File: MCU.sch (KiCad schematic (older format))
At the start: 32 parts, among them SW200 SW_SPDT, U200 STM32F405RGT6, U201 W25N01GVZEIG, Y200 16MHz

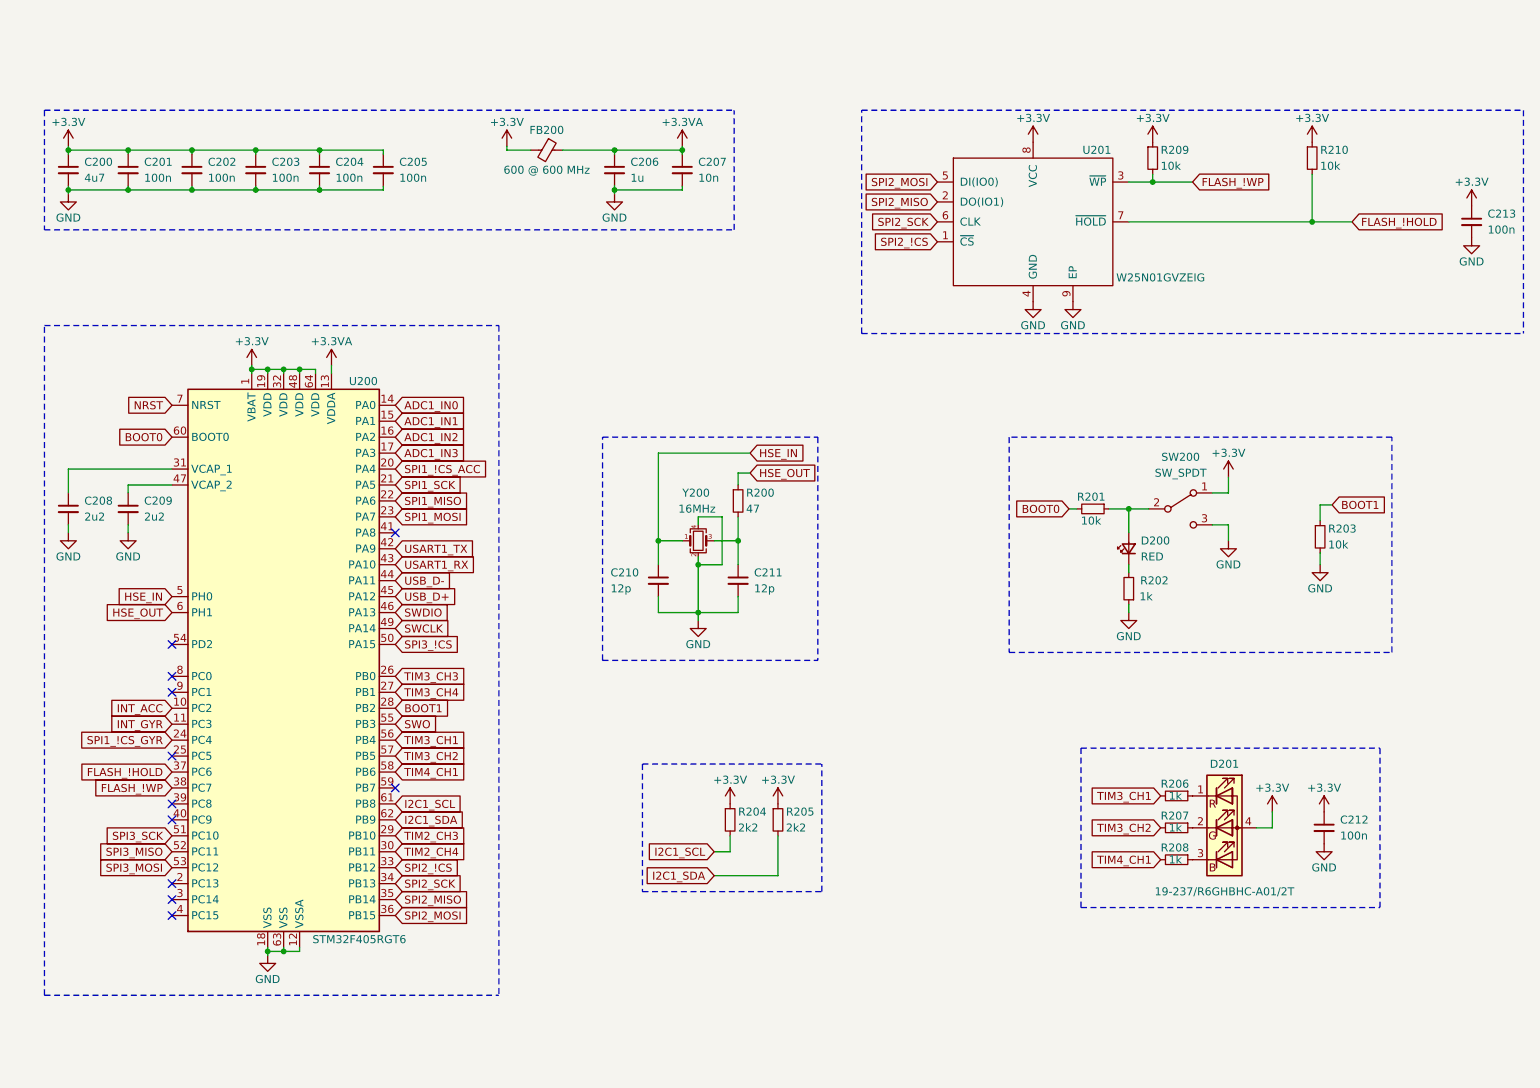
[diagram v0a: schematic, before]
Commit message: Updated firmware. Added schematic PDF.
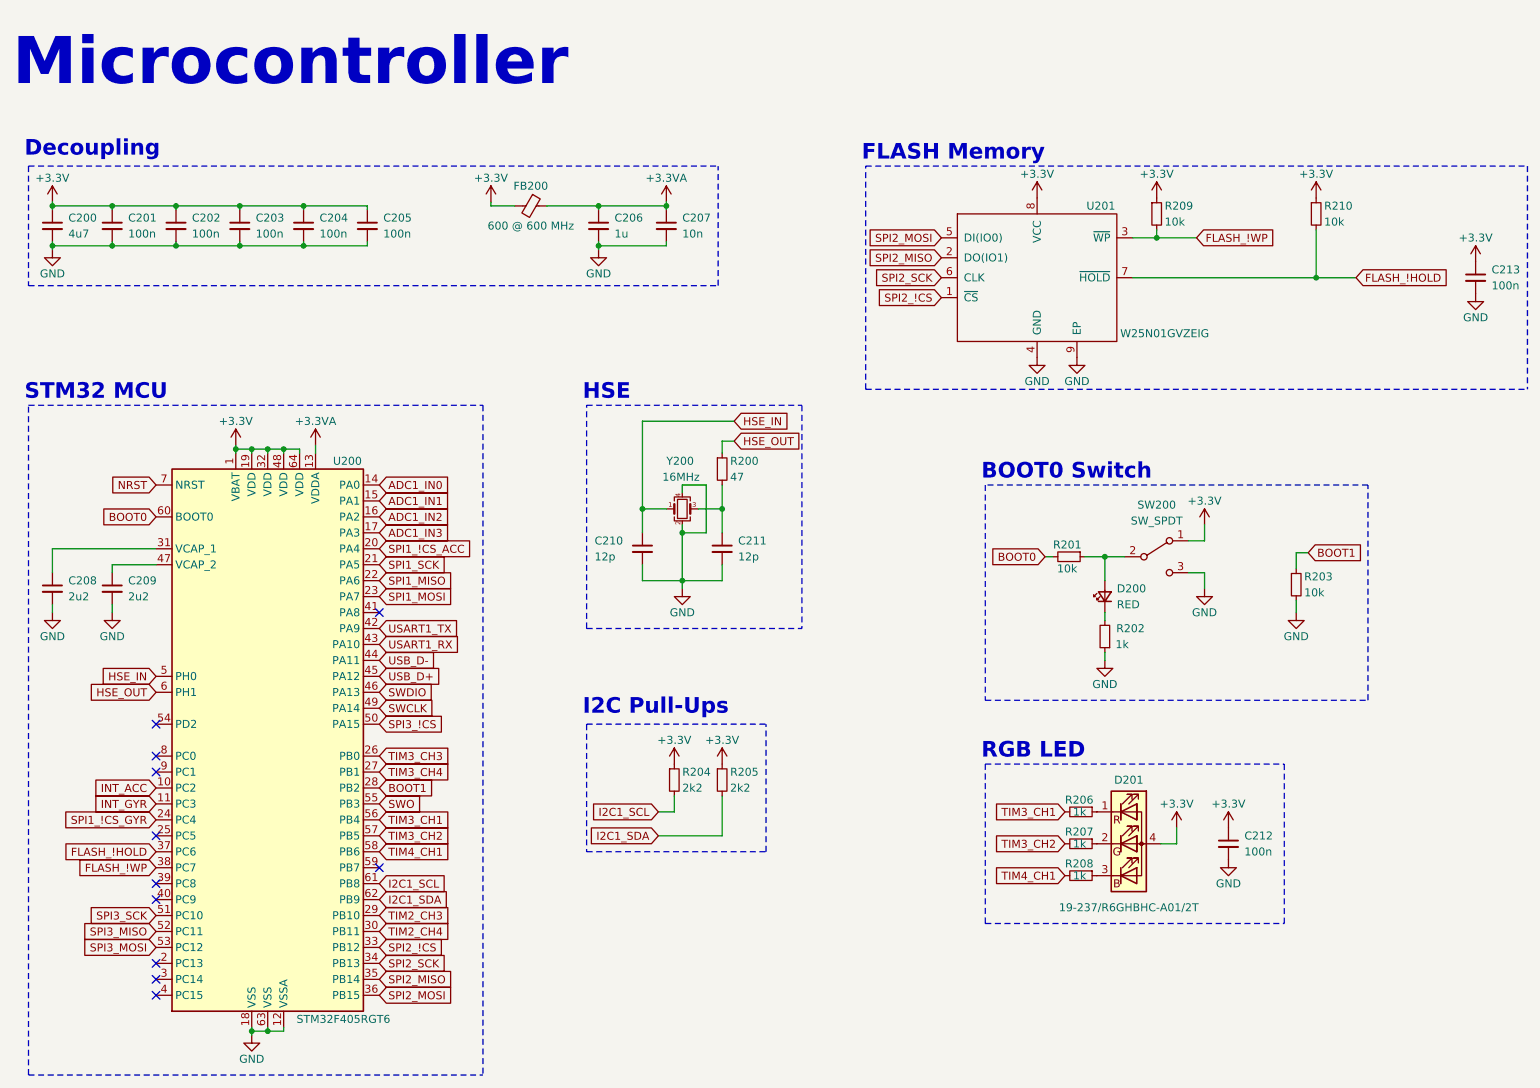
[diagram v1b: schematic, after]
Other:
- note added: "BOOT0 Switch"
- note added: "Decoupling"
- note added: "FLASH Memory"
- note added: "HSE"
- note added: "I2C Pull-Ups"
- note added: "Microcontroller"
- note added: "RGB LED"
- note added: "STM32 MCU"
- moved on the sheet: C200, C201, C202, C203, C204, C205, C206, C207, C208, C209, C210, C211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
